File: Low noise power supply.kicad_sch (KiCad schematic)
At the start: 0 parts

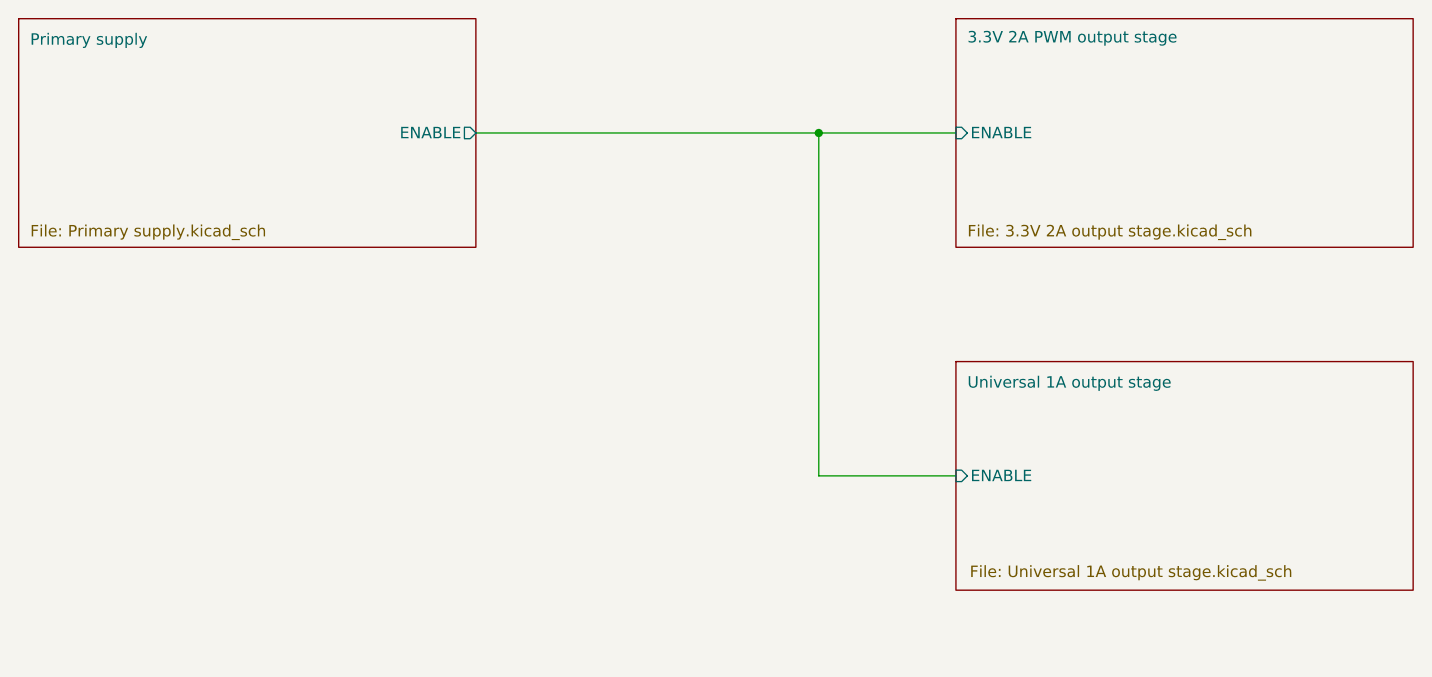
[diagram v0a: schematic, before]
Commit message: Separate 3.3V 1A pwm output stage to another sheet
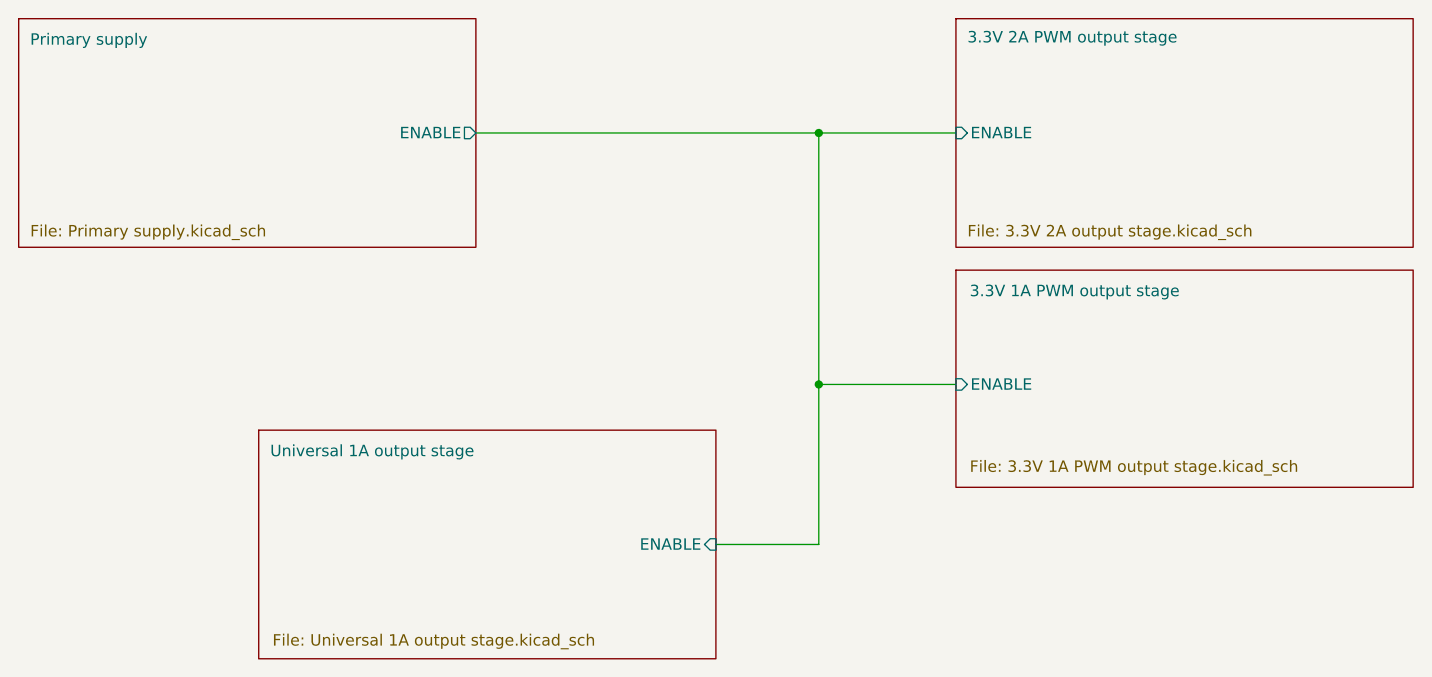
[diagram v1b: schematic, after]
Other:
- added sheet 3.3V 1A PWM output stage (3.3V 1A PWM output stage.kicad_sch)
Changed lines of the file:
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@@
 	(paper "A3")
+	(junction
+		(at 114.3 66.04)
+		(diameter 0)
+		(color 0 0 0 0)
+	)
 	(junction
 		(at 114.3 38.1)
@@
 	(wire
 		(pts
-			(xy 114.3 38.1) (xy 114.3 76.2)
+			(xy 102.87 83.82) (xy 114.3 83.82)
+		)
+		(stroke
+			(width 0)
+			(type default)
+		)
+	)
+	(wire
+		(pts
+			(xy 114.3 66.04) (xy 114.3 83.82)
 		)
 		(stroke
@@
 	(wire
 		(pts
+			(xy 129.54 66.04) (xy 114.3 66.04)
+		)
+		(stroke
+			(width 0)
+			(type default)
+		)
+	)
+	(wire
+		(pts
 			(xy 114.3 38.1) (xy 129.54 38.1)
 		)
@@
 	(wire
 		(pts
-			(xy 129.54 76.2) (xy 114.3 76.2)
+			(xy 114.3 38.1) (xy 114.3 66.04)
 		)
 		(stroke
@@
 	)
 	(sheet
-		(at 129.54 63.5)
+		(at 129.54 53.34)
+		(size 50.8 24.13)
+		(exclude_from_sim no)
+		(in_bom yes)
+		(on_board yes)
+		(dnp no)
+		(stroke
+			(width 0.1524)
+			(type solid)
+		)
+		(fill
+			(color 0 0 0 0)
+		)
+		(property "Sheetname" "3.3V 1A PWM output stage"
+			(at 131.064 56.388 0)
+			(show_name no)
+			(do_not_autoplace no)
+			(effects
+				(font
+					(size 1.27 1.27)
+				)
+				(justify left bottom)
+			)
+		)
+		(property "Sheetfile" "3.3V 1A PWM output stage.kicad_sch"
+			(at 131.064 74.422 0)
+			(show_name no)
+			(do_not_autoplace no)
+			(effects
+				(font
+					(size 1.27 1.27)
+				)
+				(justify left top)
+			)
+		)
+		(pin "ENABLE" input
+			(at 129.54 66.04 180)
+			(effects
+				(font
+					(size 1.27 1.27)
+				)
+				(justify left)
+			)
+		)
+		(instances
+			(project "Low noise power supply"
+				(path "/fca69f12-2166-43a7-ac92-c50992f66d73"
+					(page "4")
+				)
+			)
+		)
+	)
+	(sheet
+		(at 52.07 71.12)
 		(size 50.8 25.4)
 		(exclude_from_sim no)
@@
 		)
 		(property "Sheetname" "Universal 1A output stage"
-			(at 130.81 66.548 0)
+			(at 53.34 74.168 0)
 			(show_name no)
 			(do_not_autoplace no)
@@
 		)
 		(property "Sheetfile" "Universal 1A output stage.kicad_sch"
-			(at 131.064 86.106 0)
+			(at 53.594 93.726 0)
 			(show_name no)
 			(do_not_autoplace no)
@@
 		)
 		(pin "ENABLE" input
-			(at 129.54 76.2 180)
-			(effects
-				(font
-					(size 1.27 1.27)
-				)
-				(justify left)
-			)
-		)
+			(at 102.87 83.82 0)
+			(effects
+				(font
+					(size 1.27 1.27)
+				)
+				(justify right)
+			)
+		)
